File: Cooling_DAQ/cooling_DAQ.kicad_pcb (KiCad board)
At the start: 2 copper layers, 51 x 51 mm, 66 parts, among them J1 PROG, J10 PUMP_PWR, J11 FAN_PWR, J12 FAN_PWM, J2 Temp_1, J3 Temp_2, J4 PT, J5 Flow, J6 PWR, J7 USB_C_Receptacle_USB2.0_16P, J8 PUMP_PWM, J9 CAN, Q1 2N7002, Q2 2N7002, SW1 SW_SPST, U1 STM32F103C8Tx, U2 AP2204K-ADJ, U3 AP2204K-ADJ, U4 SN65HVD256D, Y1 8M, Y2 32.768k

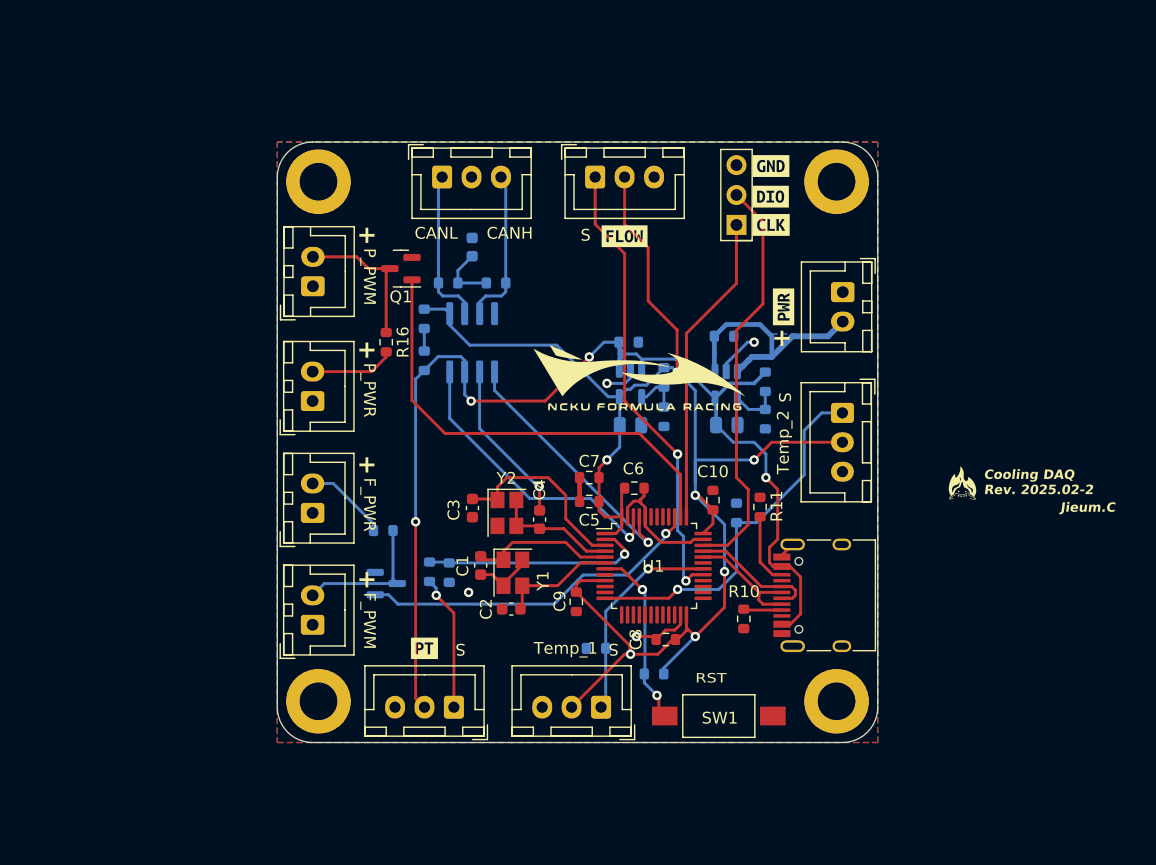
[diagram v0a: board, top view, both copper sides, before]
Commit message: update cooling DAQ
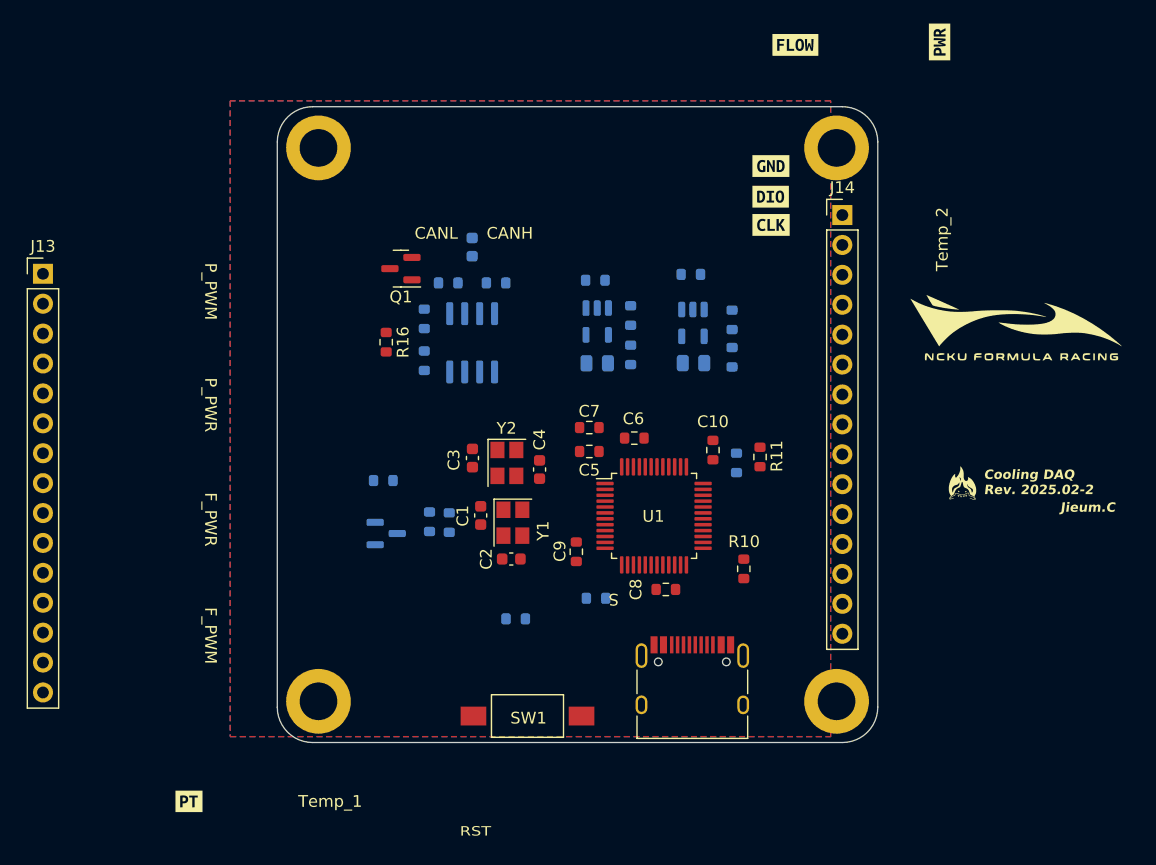
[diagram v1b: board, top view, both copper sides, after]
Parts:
- removed J1: PROG, Connector_PinHeader_2.54mm:PinHeader_1x03_P2.54mm_Vertical
- removed J10: PUMP_PWR, Connector_JST:JST_XH_B2B-XH-A_1x02_P2.50mm_Vertical
- removed J11: FAN_PWR, Connector_JST:JST_XH_B2B-XH-A_1x02_P2.50mm_Vertical
- removed J12: FAN_PWM, Connector_JST:JST_XH_B2B-XH-A_1x02_P2.50mm_Vertical
- removed J2: Temp_1, Connector_JST:JST_XH_B3B-XH-A_1x03_P2.50mm_Vertical
- removed J3: Temp_2, Connector_JST:JST_XH_B3B-XH-A_1x03_P2.50mm_Vertical
- removed J4: PT, Connector_JST:JST_XH_B3B-XH-A_1x03_P2.50mm_Vertical
- removed J5: Flow, Connector_JST:JST_XH_B3B-XH-A_1x03_P2.50mm_Vertical
- removed J6: PWR, Connector_JST:JST_XH_B2B-XH-A_1x02_P2.50mm_Vertical
- removed J8: PUMP_PWM, Connector_JST:JST_XH_B2B-XH-A_1x02_P2.50mm_Vertical
- removed J9: CAN, Connector_JST:JST_XH_B3B-XH-A_1x03_P2.50mm_Vertical
- added J13: Conn_01x15_Pin, Connector_PinHeader_2.54mm:PinHeader_1x15_P2.54mm_Vertical, F.Cu at (91.1, 104.2)
- added J14: Conn_01x15_Pin, Connector_PinHeader_2.54mm:PinHeader_1x15_P2.54mm_Vertical, F.Cu at (159.0, 99.2)
- moved G*** 32.3 mm to (173.8, 108.8)
- moved kibuzzard-67A37DFE 26.1 mm to (167.2, 84.5)
- moved kibuzzard-67A37E0F 23.9 mm to (103.5, 149.0)
- moved kibuzzard-67A37DD4 21.8 mm to (155.0, 84.8)
- moved SW1 16.2 mm to (132.2, 141.8)
- moved J7 14.3 mm to (146.2, 139.8), turned to 0 degrees
- moved R5 12.6 mm to (131.2, 133.5)
- moved C11 5.97 mm to (146.1, 104.2)
- moved C12 5.97 mm to (138.0, 104.7)
- moved C13 5.97 mm to (146.4, 111.8)
- moved C14 5.97 mm to (138.2, 111.8)
- moved R6 5.97 mm to (149.6, 111.3)
- moved R7 5.97 mm to (141.0, 111.1)
- moved R8 5.97 mm to (149.6, 108.1)
- moved R9 5.97 mm to (141.0, 107.7)
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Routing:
- net +3V3: track 138.4 -> 0.00 mm, vias 7 -> 0
- net +5V: track 97.8 -> 0.00 mm, vias 4 -> 0
- net GND: track 47.8 -> 0.00 mm, vias 5 -> 0
- net PWM_OUT: track 39.3 -> 0.00 mm
- net TIM1_CH1: track 39.2 -> 0.00 mm, vias 2 -> 0
- net SYS_JTMS-SWDIO: track 34.8 -> 0.00 mm
- net USART2: track 31.3 -> 0.00 mm, vias 1 -> 0
- net PWM_OUT_2: track 29.5 -> 0.00 mm, vias 1 -> 0
- net SYS_JTCK-SWCLK: track 26.6 -> 0.00 mm
- net CAN_RX: track 25.3 -> 0.00 mm, vias 1 -> 0
- net CAN_TX: track 22.4 -> 0.00 mm, vias 1 -> 0
- net VDC: track 20.7 -> 0.00 mm
- net ADC_CH1: track 19.3 -> 0.00 mm, vias 1 -> 0
- net USART1: track 18.1 -> 0.00 mm, vias 1 -> 0
- net /LSE_IN: track 16.3 -> 0.00 mm
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- removed copper zone on B.Cu, net VDC
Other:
- board size 51 x 51 mm -> 51 x 54 mm
- board text removed: "+"

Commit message: finish DAQ ver.1
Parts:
- removed J13, J14: Conn_01x15_Pin, Connector_PinHeader_2.54mm:PinHeader_1x15_P2.54mm_Vertical
- removed kibuzzard-67A37D2A: G***, kibuzzard-67A37D2A
- removed kibuzzard-67A37D3E: G***, kibuzzard-67A37D3E
- removed kibuzzard-67A37D8D: G***, kibuzzard-67A37D8D
- removed kibuzzard-67A37DD4: G***, kibuzzard-67A37DD4
- removed kibuzzard-67A37DFE: G***, kibuzzard-67A37DFE
- removed kibuzzard-67A37E0F: G***, kibuzzard-67A37E0F
- added J1: Conn_02x10_Odd_Even, Connector_PinHeader_2.54mm:PinHeader_2x10_P2.54mm_Vertical, B.Cu at (159.8, 108.5)
- moved SW1 48.3 mm to (147.8, 96.0)
- moved C15 38.7 mm to (154.5, 129.8)
- moved Q2 36.7 mm to (153.0, 109.8)
- moved R5 36.2 mm to (145.0, 100.0), turned to 90 degrees
- moved R13 35.8 mm to (152.5, 128.5), turned to 90 degrees
- moved R12 35.4 mm to (152.5, 132.0), turned to 90 degrees
- moved R14 34.8 mm to (153.6, 112.8), turned to 0 degrees
- moved G*** 34.6 mm to (145.5, 128.8)
- moved R16 34.3 mm to (153.5, 118.2), turned to 0 degrees
- moved Q1 33.8 mm to (153.2, 115.2), turned to 0 degrees
- moved C17 31.8 mm to (149.5, 126.2), turned to 180 degrees
- moved G*** 31.0 mm to (145.5, 102.0)
- moved R2 29.1 mm to (152.8, 121.2)
- moved U4 28.2 mm to (147.5, 130.0), turned to 0 degrees
- moved C16 26.7 mm to (142.5, 130.2)
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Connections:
- net Net-(J12-Pin_2) renamed FAN_PWM
- net Net-(J8-Pin_2) renamed PUMP_PWM
- R14 pad 2: Net-(J11-Pin_2) -> FAN_PWR
- R16 pad 2: Net-(J10-Pin_2) -> PUMP_PWR
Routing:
- net +5V: track 0.00 -> 85.6 mm, vias 0 -> 1
- net +3V3: track 0.00 -> 73.3 mm, vias 0 -> 4
- net GND: track 0.00 -> 35.5 mm
- net Net-(SW1-B): track 0.00 -> 29.4 mm, vias 0 -> 2
- net TIM1_CH1: track 0.00 -> 26.6 mm, vias 0 -> 1
- net USART2: track 0.00 -> 26.1 mm, vias 0 -> 1
- net USART1: track 0.00 -> 24.1 mm, vias 0 -> 1
- net USB_D+: track 0.00 -> 22.1 mm
- net SYS_JTMS-SWDIO: track 0.00 -> 19.8 mm
- net CAN_TX: track 0.00 -> 19.5 mm, vias 0 -> 1
- net USB_D-: track 0.00 -> 19.3 mm
- net CAN_RX: track 0.00 -> 14.5 mm, vias 0 -> 1
- net PWM_OUT_2: track 0.00 -> 14.1 mm, vias 0 -> 1
- net /LSE_OUT: track 0.00 -> 13.9 mm
- net ADC_CH1: track 0.00 -> 13.2 mm, vias 0 -> 1
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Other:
- board size 51 x 54 mm -> 30 x 50 mm
- board text added: "Cooling DAQ Rev. 2025.03"
- board text removed: "CANH"
- board text removed: "CANL"
- board text removed: "Cooling DAQ Rev. 2025.02-2"
- board text removed: "F_PWM"
- board text removed: "F_PWR"
- board text removed: "P_PWM"
- board text removed: "P_PWR"
- board text removed: "S"
- board text removed: "Temp_1"
- board text removed: "Temp_2"

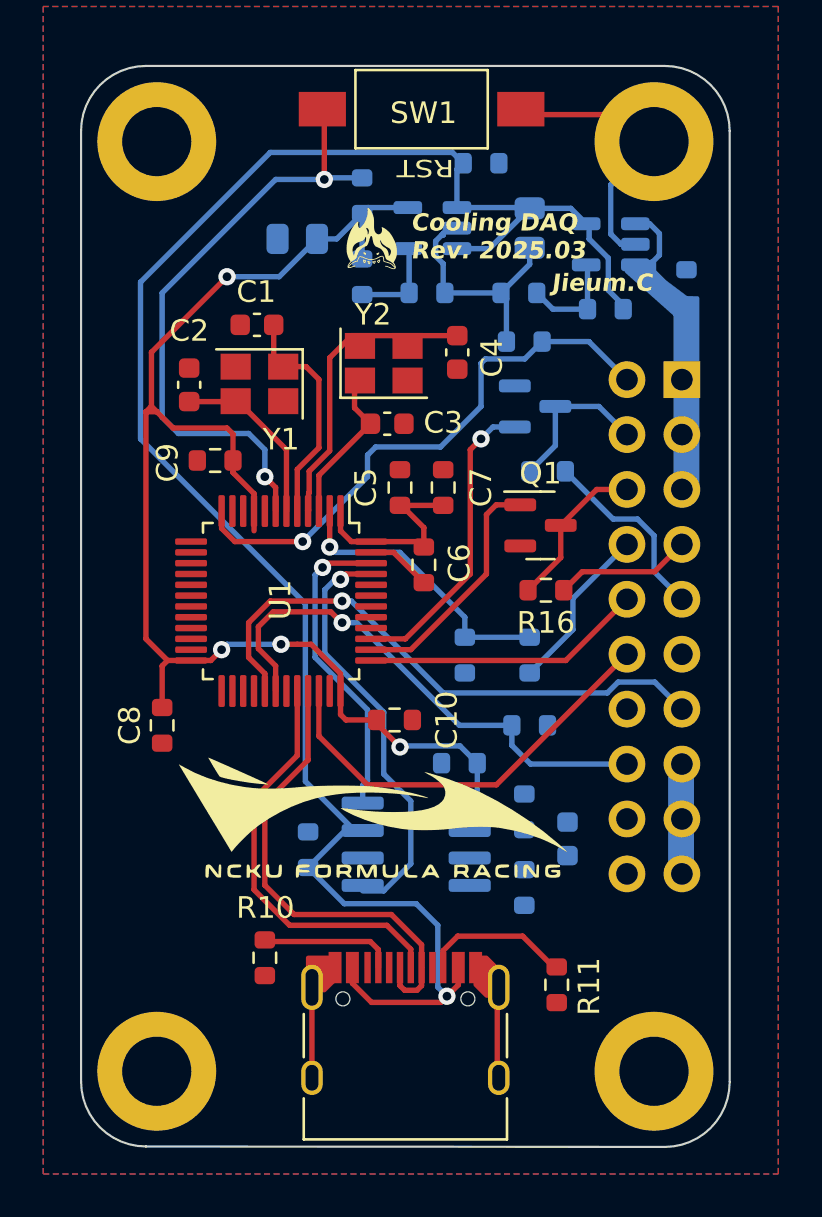
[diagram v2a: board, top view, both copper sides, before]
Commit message: finish DAQ ver.2
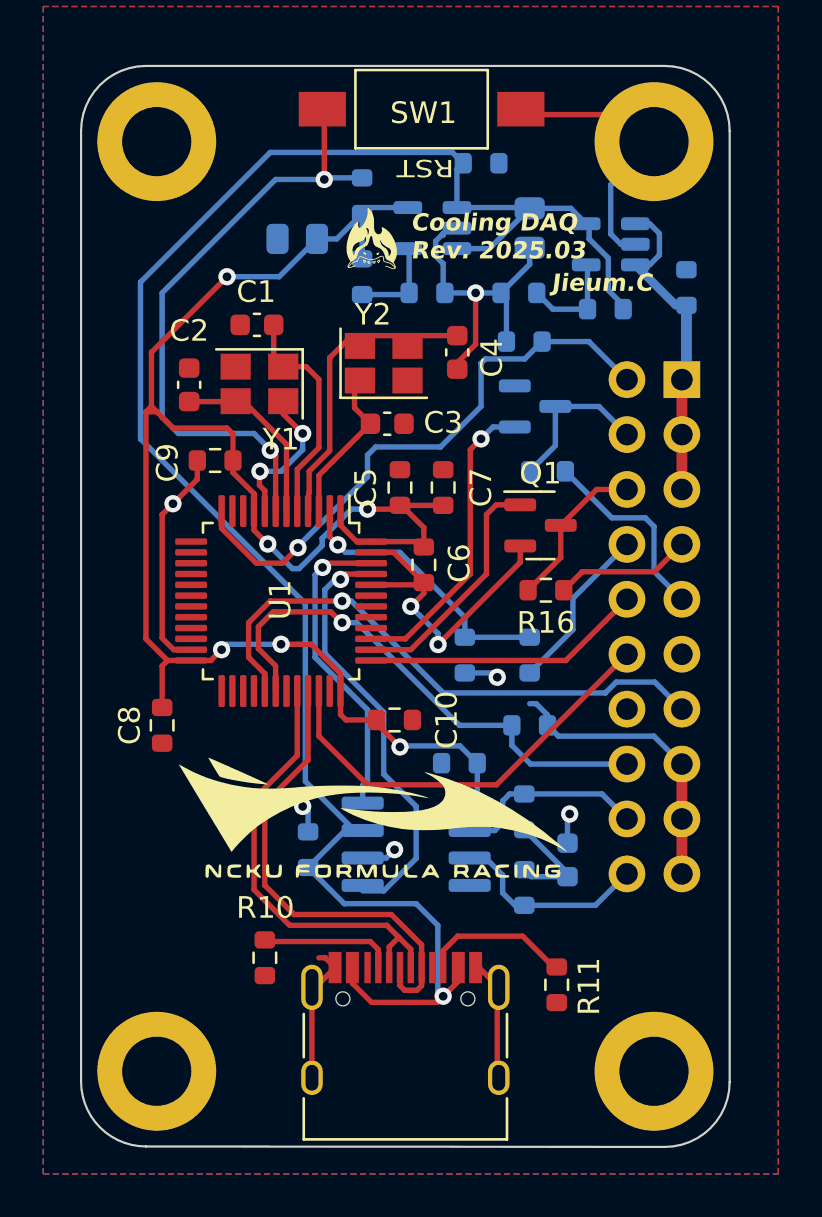
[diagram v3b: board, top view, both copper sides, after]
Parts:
- moved C15 0.97 mm to (154.5, 130.7)
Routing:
- net GND: track 35.5 -> 92.3 mm, vias 0 -> 10
- net VDC: track 3.60 -> 15.3 mm
- net CAN+: track 0.00 -> 9.27 mm
- net CAN-: track 0.00 -> 9.04 mm
- net +3V3: track 73.3 -> 82.1 mm, vias 4 -> 6
- net Net-(C15-Pad1): track 0.00 -> 5.39 mm
- net USB_D-: track 19.3 -> 20.8 mm
- net USART2: track 26.1 -> 27.0 mm
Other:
- board text removed: "S + -"

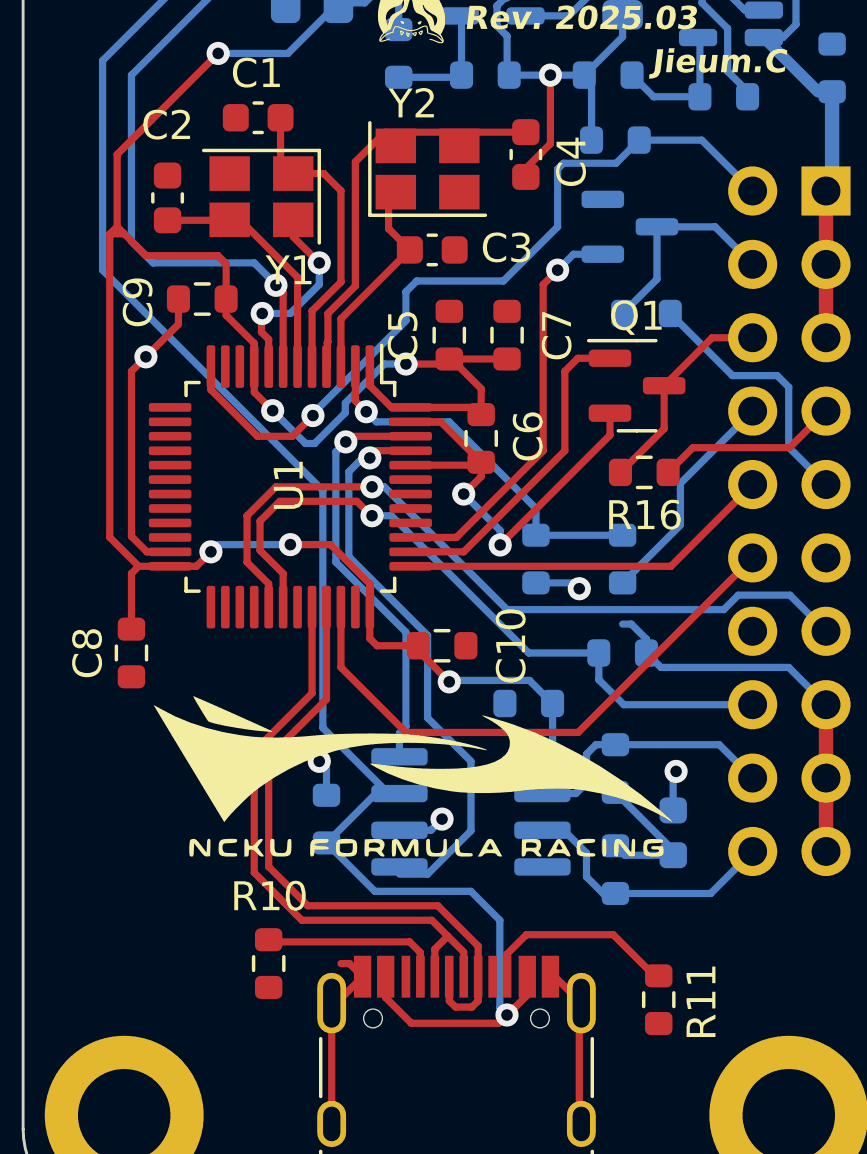
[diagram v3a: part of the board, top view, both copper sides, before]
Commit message: finish DAQ ver.2
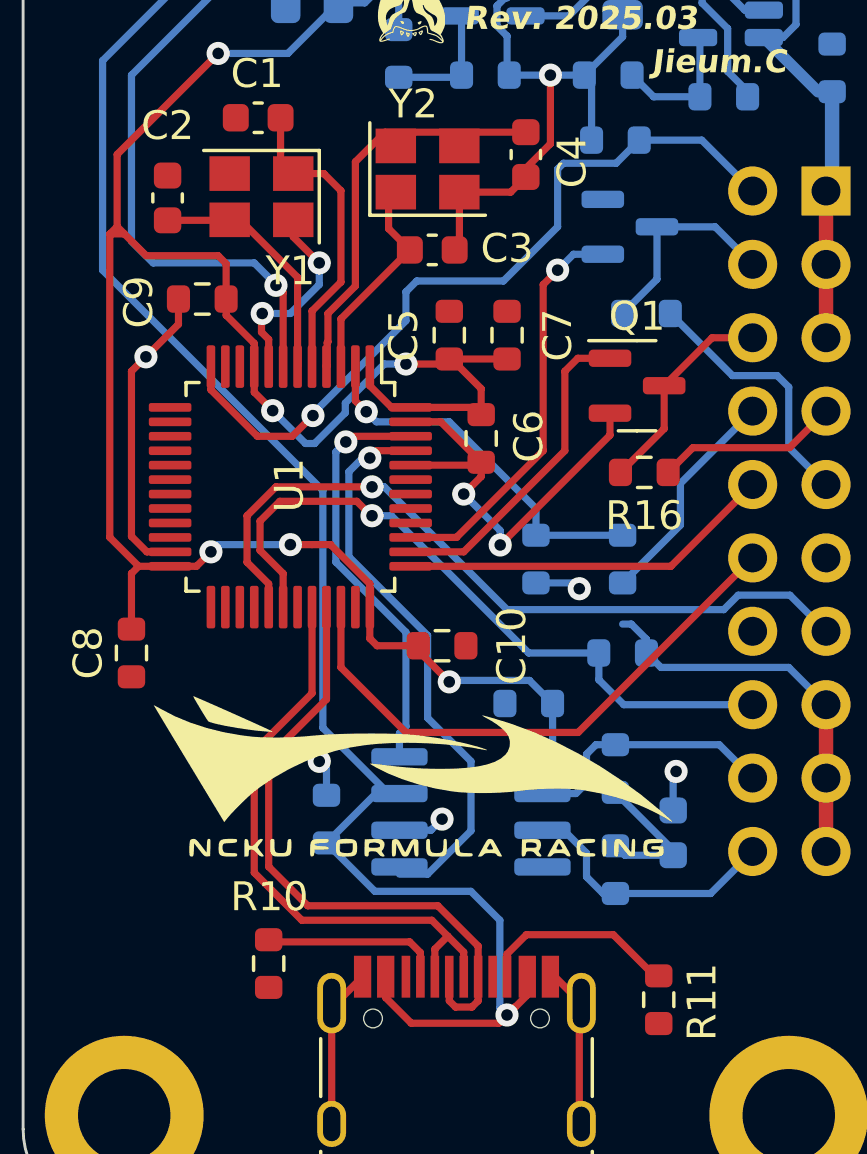
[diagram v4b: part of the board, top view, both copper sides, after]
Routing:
- net GND: track 92.3 -> 96.0 mm
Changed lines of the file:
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@@
   (segment (start 137.377 112.25) (end 137.377 113.123) (width 0.25) (layer "F.Cu") (net 2))
   (segment (start 151.25 137.601041) (end 151.675 137.176041) (width 0.25) (layer "F.Cu") (net 2))
+  (segment (start 147.1 108.55) (end 147.1 110.386) (width 0.25) (layer "F.Cu") (net 2))
   (segment (start 158.5 97.5) (end 157.25 96.25) (width 0.25) (layer "F.Cu") (net 2))
   (segment (start 140.2755 112.75) (end 140.25 112.7755) (width 0.25) (layer "F.Cu") (net 2))
@@
   (segment (start 135.75 114.75) (end 136.25 114.25) (width 0.25) (layer "F.Cu") (net 2))
   (segment (start 152.3125 116.962098) (end 148.512299 120.762299) (width 0.25) (layer "F.Cu") (net 2))
+  (segment (start 147.1 108.55) (end 148.875 108.55) (width 0.25) (layer "F.Cu") (net 2))
   (segment (start 151.675 137.176041) (end 151.675 136.823959) (width 0.25) (layer "F.Cu") (net 2))
   (segment (start 147.854 117.9) (end 147.854 118.396) (width 0.25) (layer "F.Cu") (net 2))
@@
   (segment (start 151.25 140.73) (end 151.25 137.601041) (width 0.25) (layer "F.Cu") (net 2))
   (segment (start 149.4 107.727818) (end 150.25 106.877818) (width 0.25) (layer "F.Cu") (net 2))
-  (segment (start 143.75 135.705) (end 143.295 135.25) (width 0.25) (layer "F.Cu") (net 2))
   (segment (start 152.3125 116.2) (end 152.3125 116.962098) (width 0.25) (layer "F.Cu") (net 2))
   (segment (start 151.32 140.8) (end 151.25 140.73) (width 0.25) (layer "F.Cu") (net 2))
@@
   (segment (start 137.377 113.123) (end 136.25 114.25) (width 0.25) (layer "F.Cu") (net 2))
   (segment (start 140.5 113.647918) (end 140.5 114.5875) (width 0.25) (layer "F.Cu") (net 2))
+  (segment (start 148.875 108.55) (end 149.4 108.025) (width 0.25) (layer "F.Cu") (net 2))
   (segment (start 157.25 96.25) (end 152.59 96.25) (width 0.25) (layer "F.Cu") (net 2))
   (segment (start 146.454 116.5) (end 145.4125 116.5) (width 0.25) (layer "F.Cu") (net 2))
   (segment (start 137.0875 121) (end 136.284314 121) (width 0.25) (layer "F.Cu") (net 2))
-  (segment (start 143.295 135.25) (end 143 135.25) (width 0.25) (layer "F.Cu") (net 2))
   (segment (start 136.284314 121) (end 135.75 120.465686) (width 0.25) (layer "F.Cu") (net 2))
   (segment (start 135.75 120.465686) (end 135.75 114.75) (width 0.25) (layer "F.Cu") (net 2))
   (segment (start 150.25 106.877818) (end 150.25 104.5) (width 0.25) (layer "F.Cu") (net 2))
   (segment (start 147.754 118) (end 147.854 117.9) (width 0.25) (layer "F.Cu") (net 2))
+  (segment (start 147.1 110.386) (end 146.936 110.55) (width 0.25) (layer "F.Cu") (net 2))
   (segment (start 150.25 135.705) (end 150.405 135.705) (width 0.25) (layer "F.Cu") (net 2))
   (via (at 148.512299 120.762299) (size 0.8) (drill 0.4) (layers "F.Cu" "B.Cu") (net 2))
